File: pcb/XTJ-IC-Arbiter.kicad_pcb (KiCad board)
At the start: 2 copper layers, 80.2 x 67.8 mm, 56 parts, among them IC1 SN74LV125AN, J3 DTM13-12PA-R008, Q1 NPN, U1 LM2675N-5.0/NOPB, U2 CDP68HC68S1, U3 EEC-325X4A, U4 MCP2562-H-P, U5 SP723APP, U6 MCP1700-3302E/TO

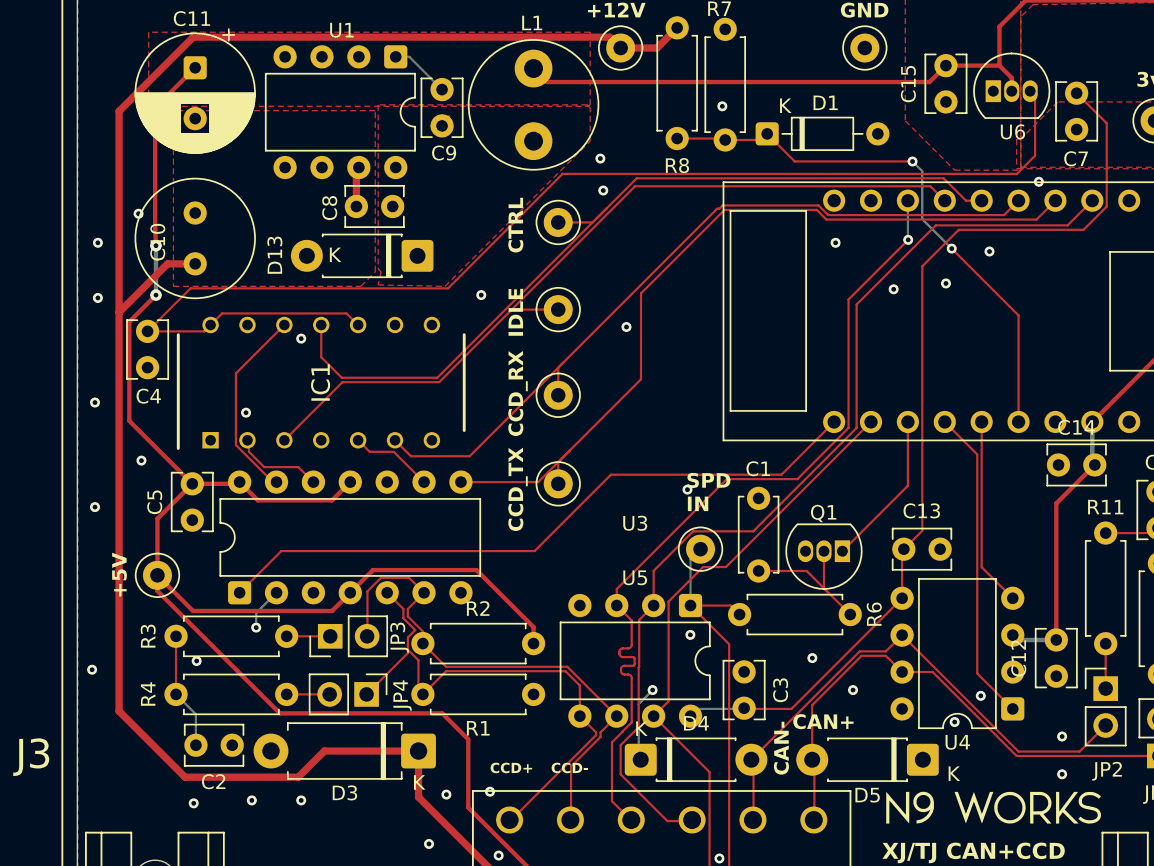
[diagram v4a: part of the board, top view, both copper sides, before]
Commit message: tie unused GPIOs to GND
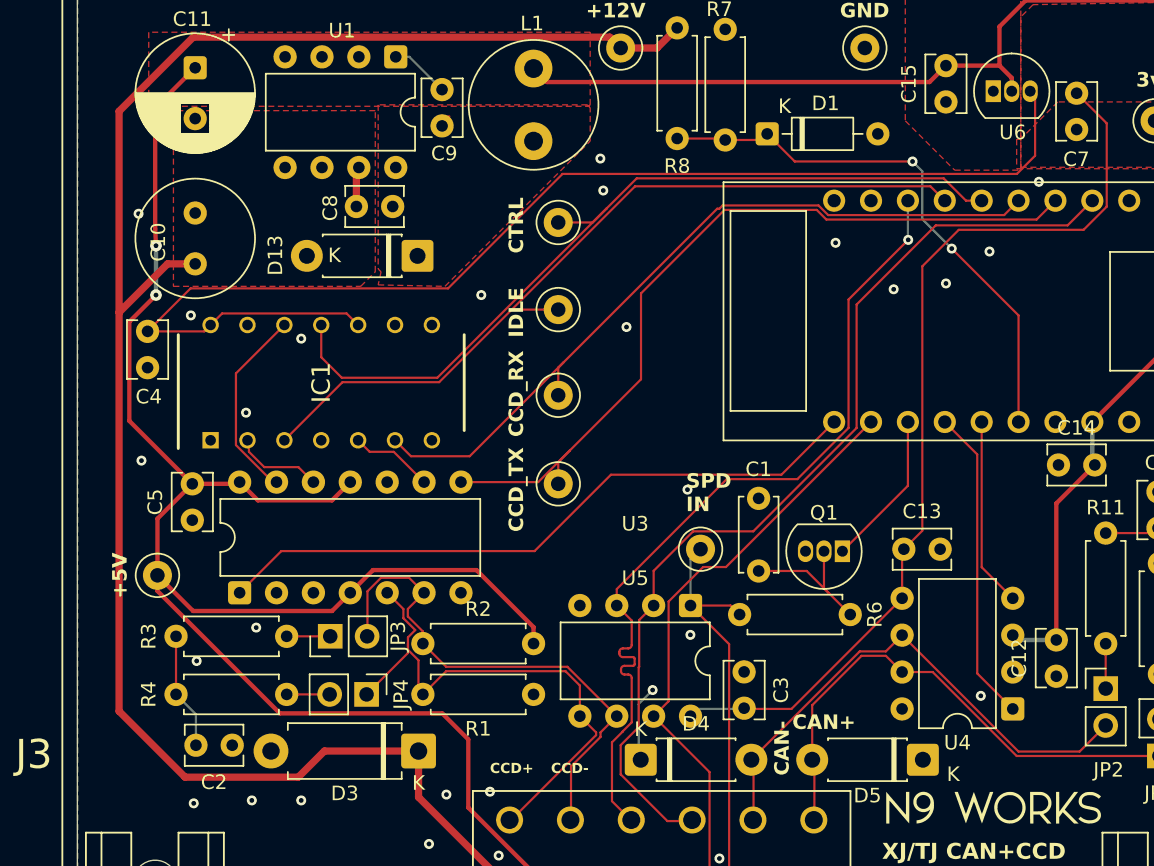
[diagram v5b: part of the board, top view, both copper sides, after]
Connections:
- XA1 pad 11: unconnected-(XA1-23-Pad11) -> GND
- XA1 pad 12: unconnected-(XA1-19-Pad12) -> GND
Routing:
- net GND: track 8.11 -> 5.13 mm, vias 39 -> 29

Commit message: dont actually connect pins to ground, as that could result in a short if the pin is configured as output
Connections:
- XA1 pad 11: GND -> unconnected-(XA1-23-Pad11)
- XA1 pad 12: GND -> unconnected-(XA1-19-Pad12)
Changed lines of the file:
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@@
 	(net 39 "idle_5v")
 	(net 40 "/CB")
+	(net 41 "unconnected-(XA1-23-Pad11)")
+	(net 42 "unconnected-(XA1-19-Pad12)")
 	(footprint "TestPoint:TestPoint_Loop_D2.50mm_Drill1.0mm"
 		(layer "F.Cu")
@@
 			(layers "*.Cu" "*.Mask")
 			(remove_unused_layers no)
-			(net 12 "GND")
+			(net 41 "unconnected-(XA1-23-Pad11)")
 			(pinfunction "23")
-			(pintype "bidirectional")
+			(pintype "bidirectional+no_connect")
 		)
 		(pad "12" thru_hole circle
@@
 			(layers "*.Cu" "*.Mask")
 			(remove_unused_layers no)
-			(net 12 "GND")
+			(net 42 "unconnected-(XA1-19-Pad12)")
 			(pinfunction "19")
-			(pintype "bidirectional")
+			(pintype "bidirectional+no_connect")
 		)
 		(pad "13" thru_hole circle

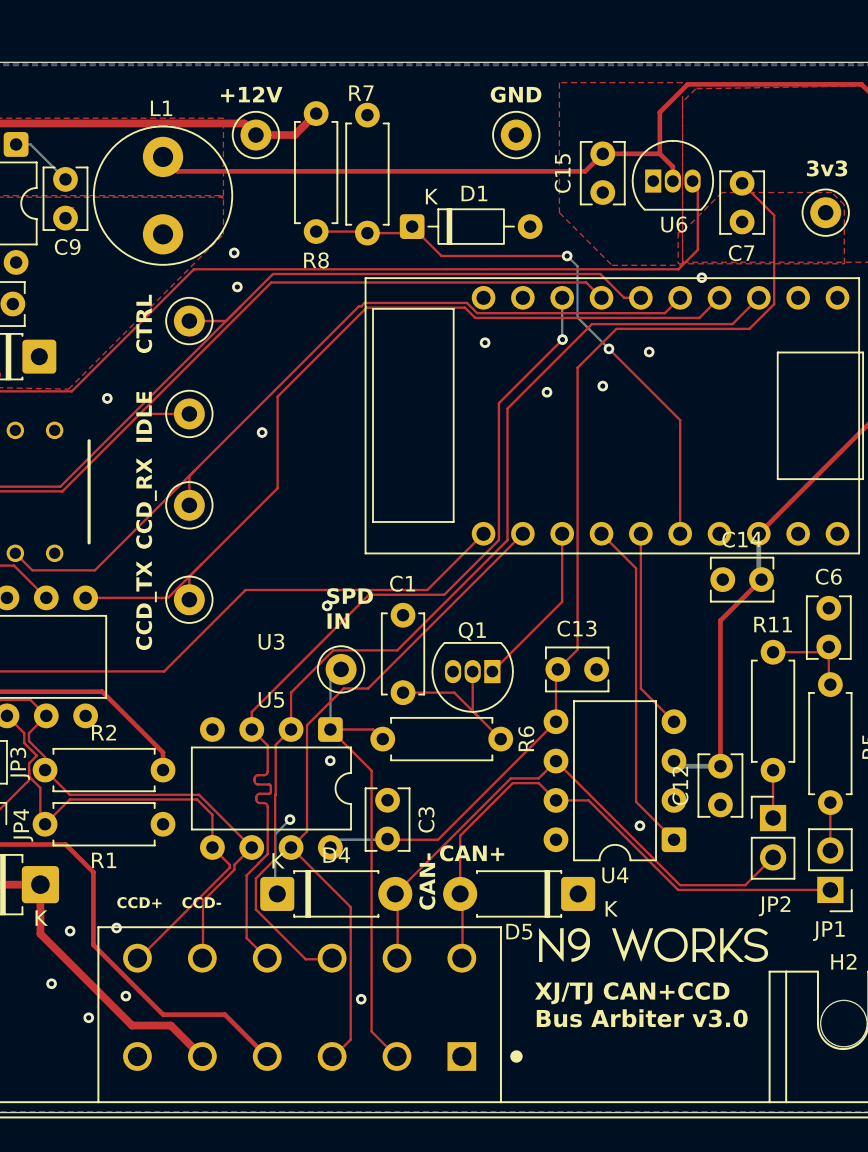
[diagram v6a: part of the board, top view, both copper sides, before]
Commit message: Get 12v measure closer to source
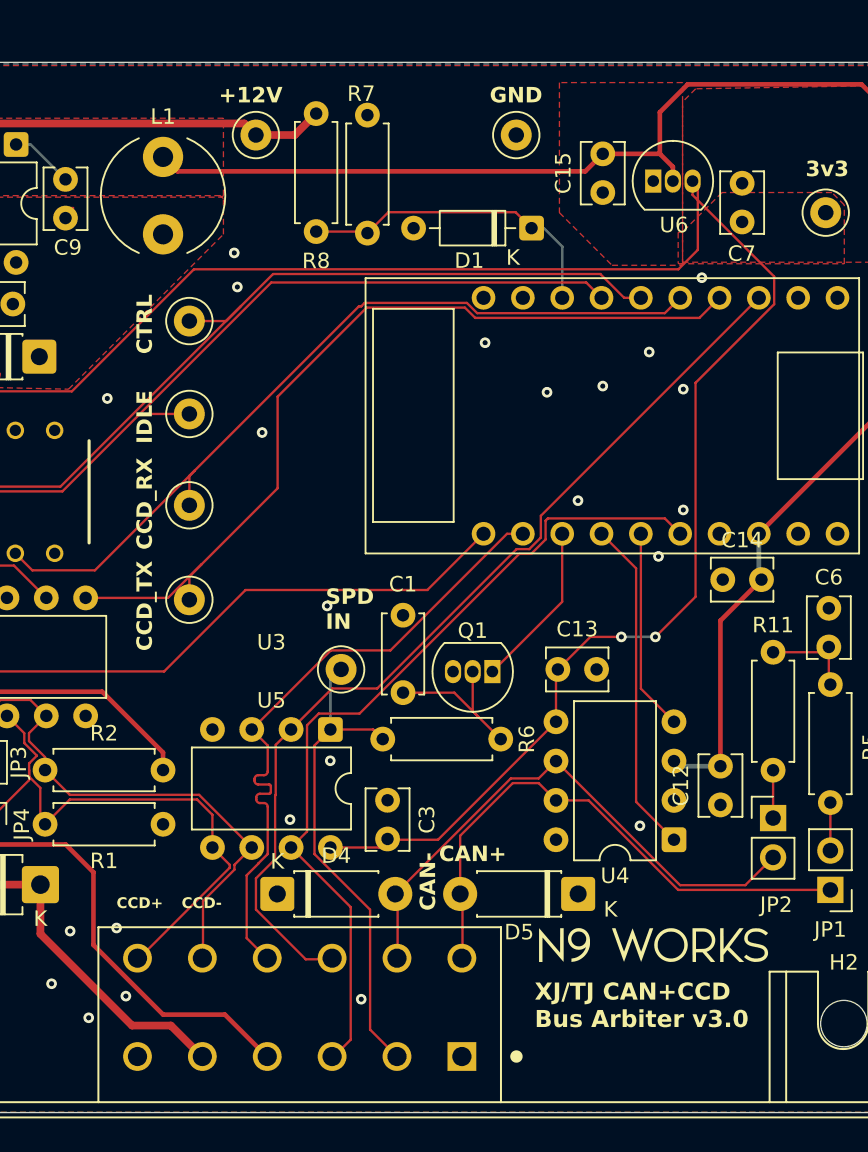
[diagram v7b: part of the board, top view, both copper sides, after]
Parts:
- L1: footprint Inductor_THT:L_Radial_D8.7mm_P5.00mm_Fastron_07HCP -> Inductor_THT:L_Radial_D7.8mm_P5.00mm_Fastron_07HCP
- moved D1 7.71 mm to (155.8, 71.0), turned to 180 degrees
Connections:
- J3 pad 3: IO/1 -> IO/3
- J3 pad 9: IO/3 -> IO/1
- U5 pad 3: IO/3 -> IO/1
- U5 pad 7: IO/1 -> IO/3
- XA1 pad 18: IO/3 -> 12V_MEASURE
- XA1 pad 6: 12V_MEASURE -> IO/3
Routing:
- net 12V_MEASURE: track 37.4 -> 20.6 mm, vias 2 -> 0
- net IO/2: track 67.0 -> 61.4 mm
- net GND: track 5.13 -> 0.07 mm, vias 29 -> 33
- net IO/3: track 58.3 -> 54.7 mm, vias 1 -> 0
- net IO/1: track 43.0 -> 41.9 mm
- net speedo_in: track 30.8 -> 31.6 mm
- net +3V3: track 149.1 -> 148.8 mm, vias 0 -> 2

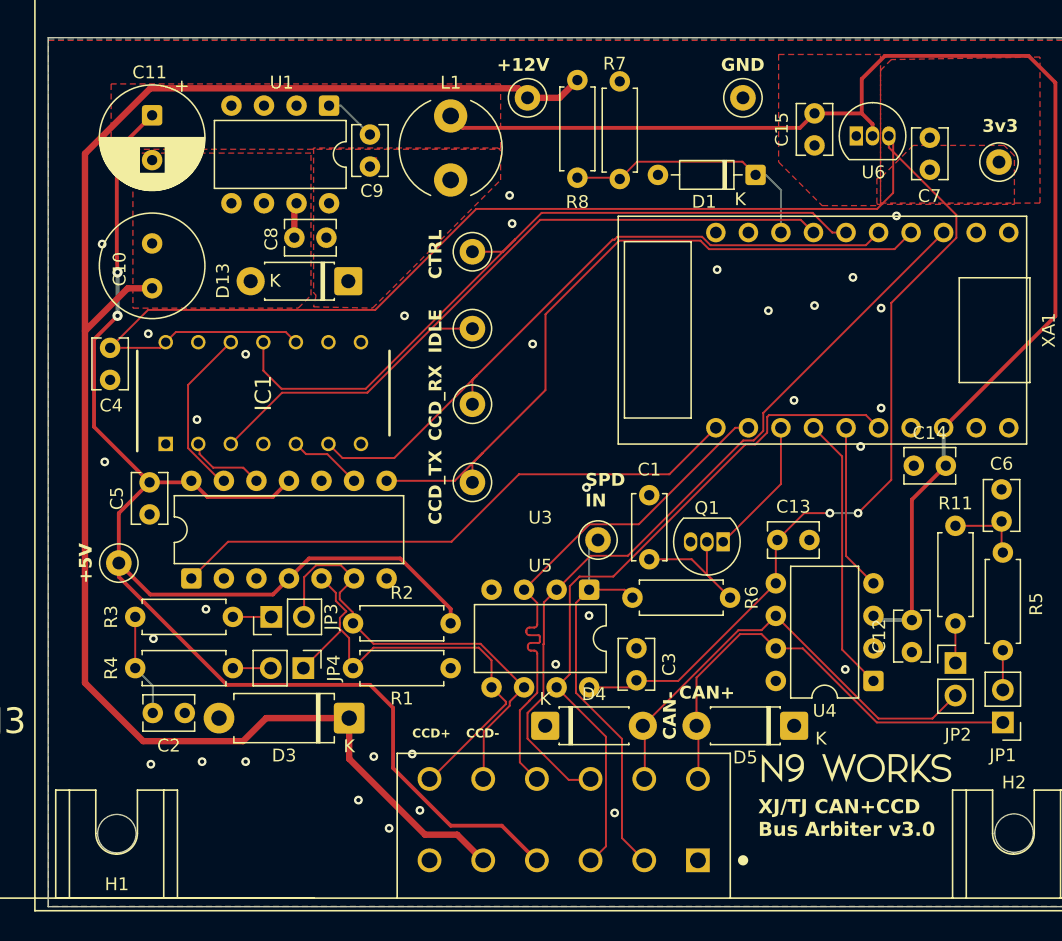
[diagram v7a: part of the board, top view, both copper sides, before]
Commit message: uniform power net, shielding via stitching
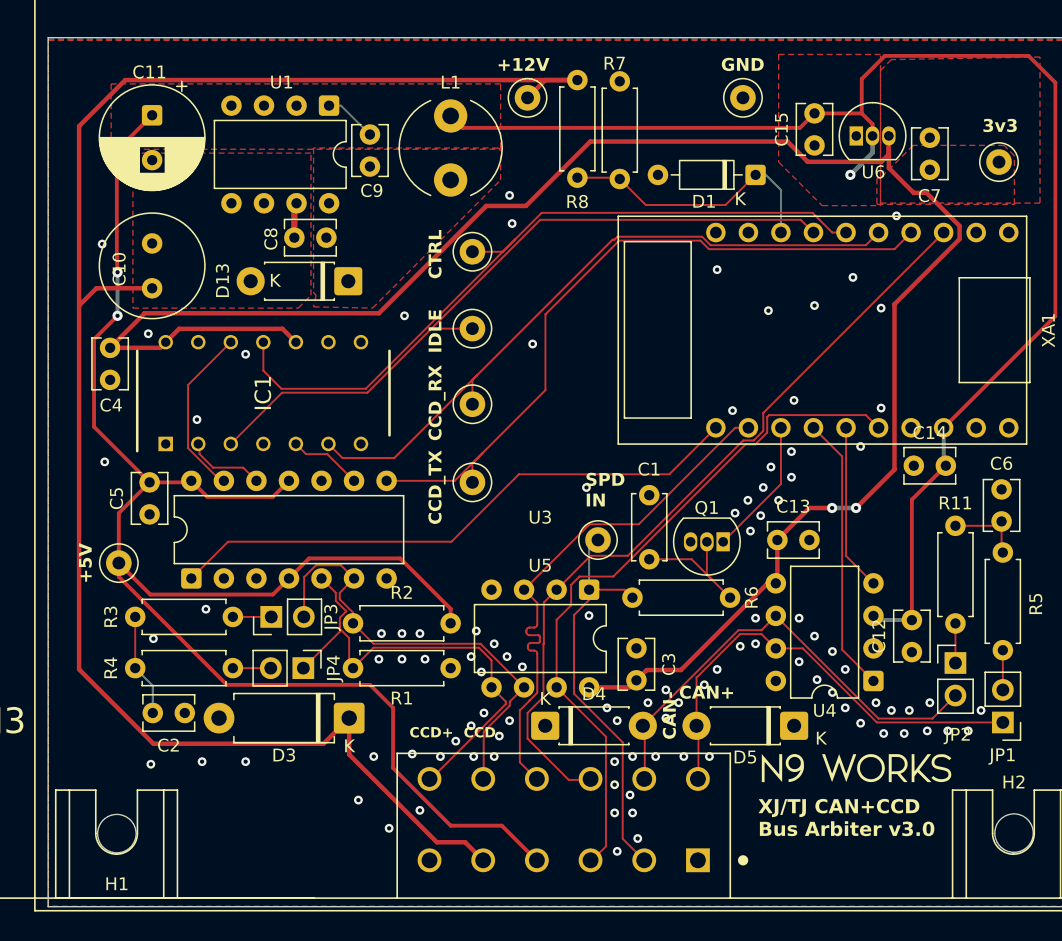
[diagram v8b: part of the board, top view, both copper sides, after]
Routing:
- net +12V: track 132.1 -> 137.1 mm
- net +5V: track 231.6 -> 235.4 mm, vias 2 -> 3
- net 12V_MEASURE: track 20.6 -> 21.4 mm
- net GND: vias 33 -> 101
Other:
- rule pad_to_mask_clearance: 0.0508 -> 0
